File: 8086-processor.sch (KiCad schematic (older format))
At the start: 20 parts

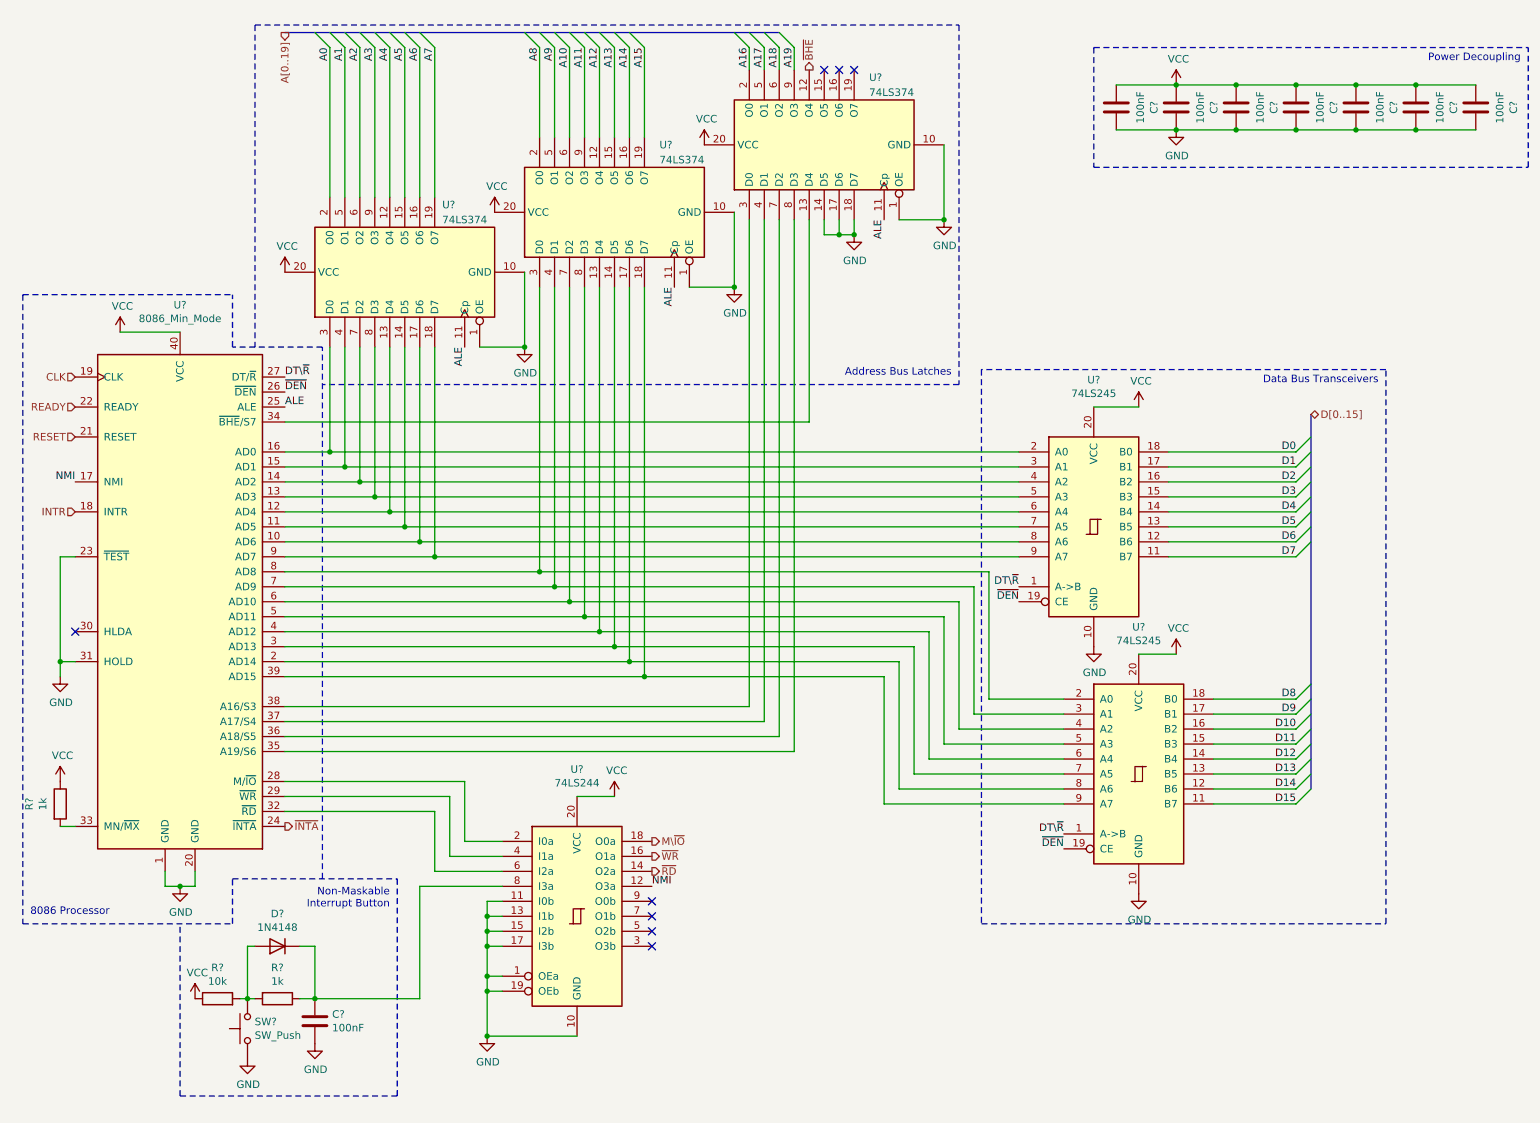
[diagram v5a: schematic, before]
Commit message: Assign footprints for most symbols
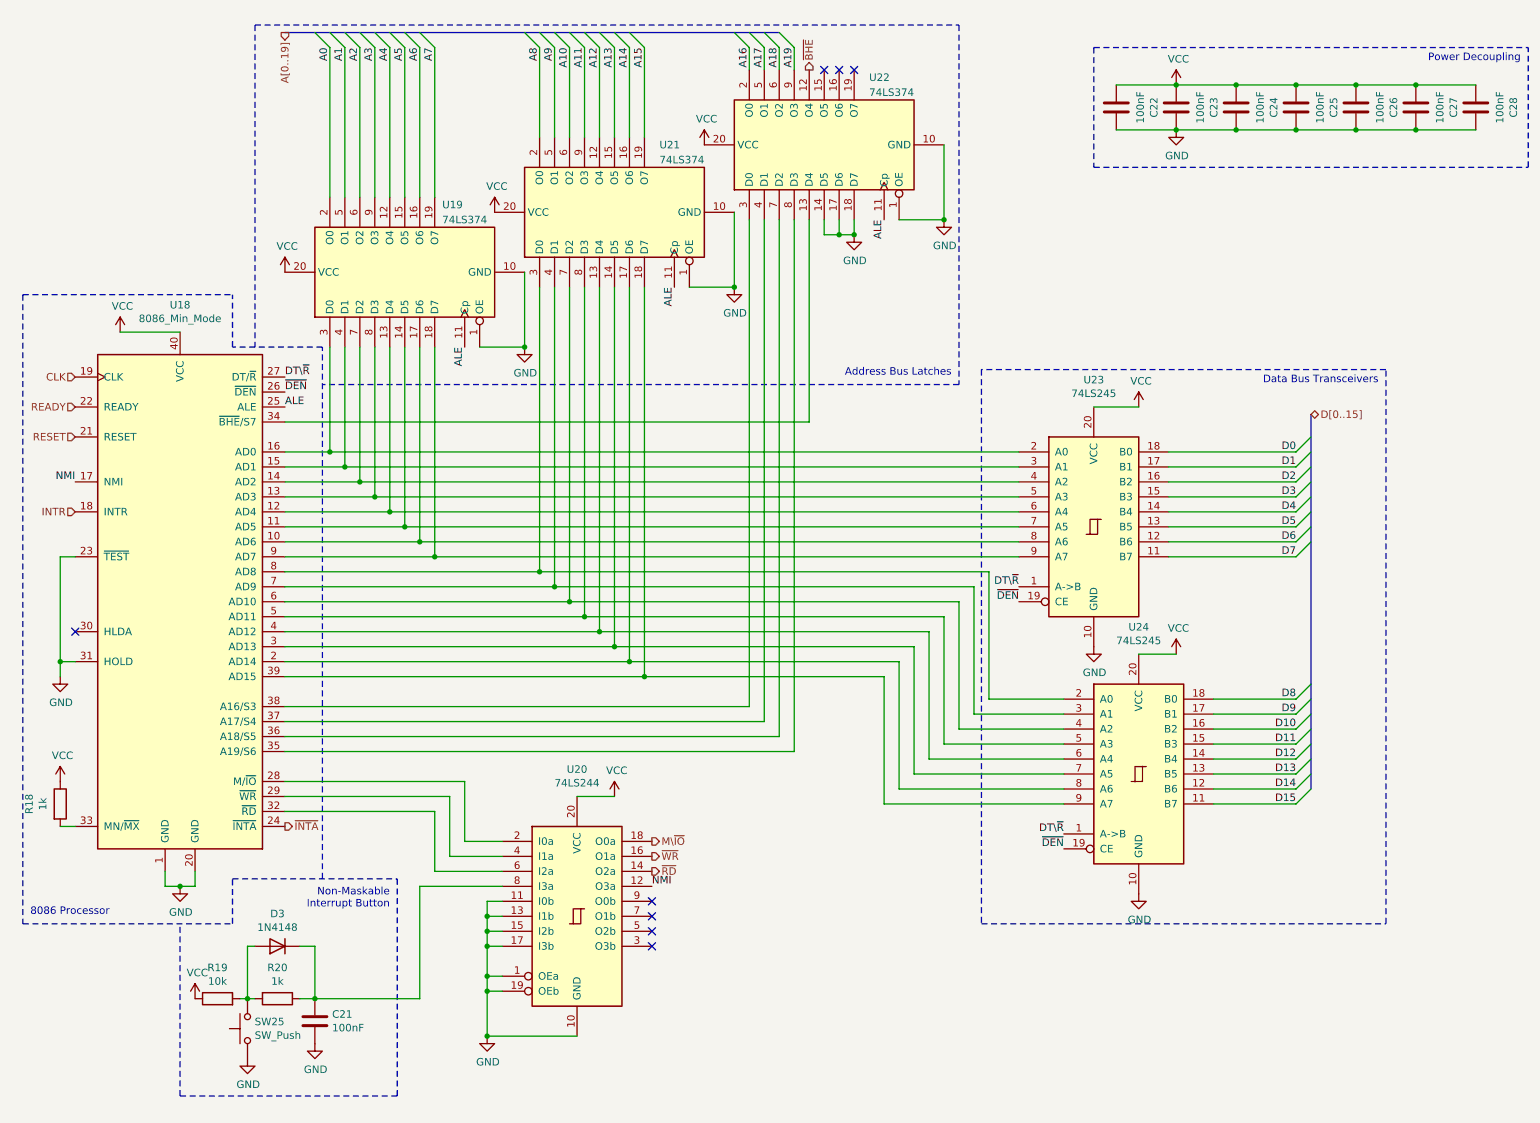
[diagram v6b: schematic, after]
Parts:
- C21, C22, C23, C24, C25, C26, C27, C28: renamed from C?; footprint (none) -> Capacitor_THT:C_Rect_L4.0mm_W2.5mm_P2.50mm
- R18, R19, R20: renamed from R?; footprint (none) -> Resistor_THT:R_Axial_DIN0207_L6.3mm_D2.5mm_P10.16mm_Horizontal
- SW25: renamed from SW?; footprint (none) -> Button_Switch_Keyboard:SW_Cherry_MX_1.00u_PCB
- U19, U20, U21, U22, U23, U24: renamed from U?; footprint (none) -> Package_DIP:DIP-20_W7.62mm
- gave numbers to parts that had none: 2

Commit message: assign footprints and edits
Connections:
- net GND: now also R19.1; no longer C21.2, SW25.1
- net VCC: now also C21.1, SW25.2; no longer R19.1
- net at R20.1, U20.8 (I3a): now also C21.2, D3.2 (A); no longer C21.1, D3.1 (K)
- net at R19.2, R20.2: now also D3.1 (K), SW25.1; no longer D3.2 (A), SW25.2
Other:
- moved on the sheet: C21, D3, SW25
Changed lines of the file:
@@
 	2300 7000 2250 7000
-$Comp
-L power:GND #PWR0191
-U 1 1 627AC8BB
-P 2700 7300
-F 0 "#PWR0191" H 2700 7050 50  0001 C CNN
-F 1 "GND" H 2705 7127 50  0000 C CNN
-F 2 "" H 2700 7300 50  0001 C CNN
-F 3 "" H 2700 7300 50  0001 C CNN
-	1    2700 7300
-	1    0    0    -1
-$EndComp
 $Comp
 L Device:R R20
@@
 F 3 "~" H 2450 7000 50  0001 C CNN
 	1    2450 7000
-	0    1    1    0
+	0    1    -1   0
 $EndComp
 $Comp
 L power:VCC #PWR0192
 U 1 1 6278DB4C
-P 1900 7000
-F 0 "#PWR0192" H 1900 6850 50  0001 C CNN
-F 1 "VCC" H 1915 7173 50  0000 C CNN
-F 2 "" H 1900 7000 50  0001 C CNN
-F 3 "" H 1900 7000 50  0001 C CNN
-	1    1900 7000
+P 2700 6700
+F 0 "#PWR0192" H 2700 6550 50  0001 C CNN
+F 1 "VCC" H 2715 6873 50  0000 C CNN
+F 2 "" H 2700 6700 50  0001 C CNN
+F 3 "" H 2700 6700 50  0001 C CNN
+	1    2700 6700
 	1    0    0    -1
 $EndComp
@@
 L Device:C C21
 U 1 1 6277FDCA
-P 2700 7150
-F 0 "C21" H 2815 7196 50  0000 L CNN
-F 1 "100nF" H 2815 7105 50  0000 L CNN
-F 2 "Capacitor_THT:C_Rect_L4.0mm_W2.5mm_P2.50mm" H 2738 7000 50  0001 C CNN
-F 3 "~" H 2700 7150 50  0001 C CNN
-	1    2700 7150
+P 2700 6850
+F 0 "C21" H 2815 6896 50  0000 L CNN
+F 1 "100nF" H 2815 6805 50  0000 L CNN
+F 2 "Capacitor_THT:C_Rect_L4.0mm_W2.5mm_P2.50mm" H 2738 6700 50  0001 C CNN
+F 3 "~" H 2700 6850 50  0001 C CNN
+	1    2700 6850
 	1    0    0    -1
 $EndComp
@@
 L Switch:SW_Push SW25
 U 1 1 626B0BE8
-P 2250 7200
-F 0 "SW25" V 2296 7152 50  0000 R CNN
-F 1 "SW_Push" V 2205 7152 50  0000 R CNN
-F 2 "Button_Switch_Keyboard:SW_Cherry_MX_1.00u_PCB" H 2250 7400 50  0001 C CNN
-F 3 "~" H 2250 7400 50  0001 C CNN
-	1    2250 7200
+P 2250 6800
+F 0 "SW25" V 2296 6752 50  0000 R CNN
+F 1 "SW_Push" V 2205 6752 50  0000 R CNN
+F 2 "Button_Switch_Keyboard:SW_Cherry_MX_1.00u_PCB" H 2250 7000 50  0001 C CNN
+F 3 "~" H 2250 7000 50  0001 C CNN
+	1    2250 6800
 	0    -1   -1   0
 $EndComp
@@
 L power:GND #PWR0193
 U 1 1 6233B1ED
-P 2250 7400
-F 0 "#PWR0193" H 2250 7150 50  0001 C CNN
-F 1 "GND" H 2255 7227 50  0000 C CNN
-F 2 "" H 2250 7400 50  0001 C CNN
-F 3 "" H 2250 7400 50  0001 C CNN
-	1    2250 7400
+P 1900 7100
+F 0 "#PWR0193" H 1900 6850 50  0001 C CNN
+F 1 "GND" H 1905 6927 50  0000 C CNN
+F 2 "" H 1900 7100 50  0001 C CNN
+F 3 "" H 1900 7100 50  0001 C CNN
+	1    1900 7100
 	1    0    0    -1
 $EndComp
@@
 L Diode:1N4148 D?
 U 1 1 61F82EF7
-P 2450 6650
+P 2450 7350
 AR Path="/61CB92C1/61F82EF7" Ref="D?"  Part="1"
 AR Path="/6190420C/61F82EF7" Ref="D3"  Part="1"
-F 0 "D3" H 2450 6433 50  0000 C CNN
-F 1 "1N4148" H 2450 6524 50  0000 C CNN
-F 2 "Diode_THT:D_DO-35_SOD27_P7.62mm_Horizontal" H 2450 6475 50  0001 C CNN
-F 3 "https://assets.nexperia.com/documents/data-sheet/1N4148_1N4448.pdf" H 2450 6650 50  0001 C CNN
-	1    2450 6650
-	-1   0    0    1
+F 0 "D3" H 2450 7133 50  0000 C CNN
+F 1 "1N4148" H 2450 7224 50  0000 C CNN
+F 2 "Diode_THT:D_DO-35_SOD27_P7.62mm_Horizontal" H 2450 7175 50  0001 C CNN
+F 3 "https://assets.nexperia.com/documents/data-sheet/1N4148_1N4448.pdf" H 2450 7350 50  0001 C CNN
+	1    2450 7350
+	1    0    0    -1
 $EndComp
 Wire Notes Line
@@
 Wire Notes Line
 	3250 7650 3250 6200
-Wire Wire Line
-	2600 6650 2700 6650
-Wire Wire Line
-	2300 6650 2250 6650
-Wire Wire Line
-	2250 6650 2250 7000
-Wire Wire Line
-	2700 6650 2700 7000
 Wire Wire Line
 	1100 4050 1000 4050
@@
 	1000 4850 1000 4750
 NoConn ~ 1100 4550
+$Comp
+L power:VCC #PWR04
+U 1 1 61B699AA
+P 2250 6600
+F 0 "#PWR04" H 2250 6450 50  0001 C CNN
+F 1 "VCC" H 2265 6773 50  0000 C CNN
+F 2 "" H 2250 6600 50  0001 C CNN
+F 3 "" H 2250 6600 50  0001 C CNN
+	1    2250 6600
+	1    0    0    -1
+$EndComp
+Wire Wire Line
+	2700 7000 2700 7350
+Wire Wire Line
+	2700 7350 2600 7350
+Wire Wire Line
+	2250 7000 2250 7350
+Wire Wire Line
+	2250 7350 2300 7350
+Wire Wire Line
+	1900 7100 1900 7000
 Wire Bus Line
 	9350 3100 9350 5600

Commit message: begin pcb layout
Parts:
- SW25: value SW_Push -> NMI
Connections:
- net A0: now also U19.9 (O3); no longer U19.2 (O0)
- net A1: now also U19.6 (O2); no longer U19.5 (O1)
- net A10: now also U21.5 (O1); no longer U21.6 (O2)
- net A11: now also U21.2 (O0); no longer U21.9 (O3)
- net A2: now also U19.5 (O1); no longer U19.6 (O2)
- net A3: now also U19.2 (O0); no longer U19.9 (O3)
- net A8: now also U21.9 (O3); no longer U21.2 (O0)
- net A9: now also U21.6 (O2); no longer U21.5 (O1)
- net at U18.13 (AD3), U23.5 (A3): now also U19.3 (D0); no longer U19.8 (D3)
- net at U18.14 (AD2), U23.4 (A2): now also U19.4 (D1); no longer U19.7 (D2)
- net at U18.15 (AD1), U23.3 (A1): now also U19.7 (D2); no longer U19.4 (D1)
- net at U18.16 (AD0), U23.2 (A0): now also U19.8 (D3); no longer U19.3 (D0)
- net at U18.5 (AD11), U24.5 (A3): now also U21.3 (D0); no longer U21.8 (D3)
- net at U18.6 (AD10), U24.4 (A2): now also U21.4 (D1); no longer U21.7 (D2)
- net at U18.7 (AD9), U24.3 (A1): now also U21.7 (D2); no longer U21.4 (D1)
- net at U18.8 (AD8), U24.2 (A0): now also U21.8 (D3); no longer U21.3 (D0)
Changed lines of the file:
@@
 ALE
 Wire Wire Line
-	2500 3750 3200 3750
-Wire Wire Line
 	6600 5600 7700 5600
 Wire Wire Line
@@
 Wire Wire Line
 	6500 4850 6500 5700
-Wire Wire Line
-	3100 2650 3100 3650
-Wire Wire Line
-	3000 2650 3000 3550
 $Comp
 L power:VCC #PWR0181
@@
 $EndComp
 Wire Wire Line
-	2800 2650 2800 3350
-Wire Wire Line
-	2900 2650 2900 3450
-Wire Wire Line
 	3800 2650 4100 2650
 Connection ~ 4100 2650
@@
 ALE
 Wire Wire Line
-	2500 3650 3100 3650
-Wire Wire Line
-	2500 3450 2900 3450
-Wire Wire Line
-	2500 3350 2800 3350
-Wire Wire Line
-	2500 3550 3000 3550
-Connection ~ 2800 3350
-Wire Wire Line
-	2800 3350 7400 3350
-Connection ~ 2900 3450
-Wire Wire Line
-	2900 3450 7400 3450
-Connection ~ 3000 3550
-Wire Wire Line
-	3000 3550 7400 3550
-Connection ~ 3100 3650
-Wire Wire Line
-	3100 3650 7400 3650
+	2500 3650 2800 3650
+Wire Wire Line
+	2500 3550 2900 3550
 Wire Wire Line
 	5600 1800 5600 5050
@@
 	5900 5350 2500 5350
 Wire Wire Line
-	2500 3850 3300 3850
-Wire Wire Line
-	2500 3950 3400 3950
-Wire Wire Line
-	2500 4050 3500 4050
-Wire Wire Line
-	2500 4150 4200 4150
-Wire Wire Line
-	2500 4250 4300 4250
-Wire Wire Line
-	2500 4350 4400 4350
-Wire Wire Line
-	2500 4650 4700 4650
-Wire Wire Line
-	2500 4850 4900 4850
-Wire Wire Line
-	3200 2650 3200 3750
-Connection ~ 3200 3750
-Wire Wire Line
-	3200 3750 7400 3750
-Wire Wire Line
-	3300 3850 3300 2650
-Connection ~ 3300 3850
-Wire Wire Line
-	3300 3850 7400 3850
-Wire Wire Line
-	3400 2650 3400 3950
-Connection ~ 3400 3950
-Wire Wire Line
-	3400 3950 7400 3950
-Wire Wire Line
-	3500 4050 3500 2650
-Connection ~ 3500 4050
-Wire Wire Line
-	3500 4050 7400 4050
-Wire Wire Line
-	2500 4750 4800 4750
-Wire Wire Line
-	2500 4550 4600 4550
-Wire Wire Line
-	2500 4450 4500 4450
-Wire Wire Line
-	4200 4150 4200 2250
-Connection ~ 4200 4150
-Connection ~ 4300 4250
-Connection ~ 4400 4350
-Connection ~ 4500 4450
-Connection ~ 4600 4550
-Connection ~ 4700 4650
-Connection ~ 4800 4750
-Wire Wire Line
-	4800 4750 6600 4750
-Wire Wire Line
-	4900 2250 4900 4850
-Connection ~ 4900 4850
-Wire Wire Line
-	4900 4850 6500 4850
-Wire Wire Line
-	4800 2250 4800 4750
-Wire Wire Line
-	4700 4650 6700 4650
-Wire Wire Line
-	4700 2250 4700 4650
-Wire Wire Line
-	4600 4550 6800 4550
-Wire Wire Line
-	4600 2250 4600 4550
-Wire Wire Line
-	4500 4450 6900 4450
-Wire Wire Line
-	4500 2250 4500 4450
-Wire Wire Line
-	4400 4350 7000 4350
-Wire Wire Line
-	4400 2250 4400 4350
-Wire Wire Line
-	4300 4250 7100 4250
-Wire Wire Line
-	4300 2250 4300 4250
-Wire Wire Line
-	4200 4150 7200 4150
+	2500 4350 4300 4350
+Wire Wire Line
+	2500 4450 4200 4450
+Wire Wire Line
+	4500 4150 4500 2250
+Wire Wire Line
+	4400 2250 4400 4250
 $Comp
 L power:VCC #PWR0185
@@
 Entry Wire Line
 	2800 650  2700 550
+Text Label 3100 650  3    50   ~ 0
+A0
+Text Label 3000 650  3    50   ~ 0
+A1
+Text Label 2900 650  3    50   ~ 0
+A2
 Text Label 2800 650  3    50   ~ 0
-A0
-Text Label 3500 650  3    50   ~ 0
-A7
-Text Label 2900 650  3    50   ~ 0
-A1
-Text Label 3000 650  3    50   ~ 0
-A2
-Text Label 3100 650  3    50   ~ 0
 A3
-Text Label 3200 650  3    50   ~ 0
-A4
-Text Label 3300 650  3    50   ~ 0
-A5
-Text Label 3400 650  3    50   ~ 0
-A6
-Text Label 4200 650  3    50   ~ 0
+Text Label 4500 650  3    50   ~ 0
 A8
+Text Label 4400 650  3    50   ~ 0
+A9
 Text Label 4300 650  3    50   ~ 0
-A9
-Text Label 4400 650  3    50   ~ 0
 A10
-Text Label 4500 650  3    50   ~ 0
-A11
-Text Label 4600 650  3    50   ~ 0
-A12
-Text Label 4700 650  3    50   ~ 0
-A13
-Text Label 4800 650  3    50   ~ 0
-A14
-Text Label 4900 650  3    50   ~ 0
-A15
 Text Label 5600 650  3    50   ~ 0
 A16
@@
 P 2250 6800
 F 0 "SW25" V 2296 6752 50  0000 R CNN
-F 1 "SW_Push" V 2205 6752 50  0000 R CNN
+F 1 "NMI" V 2205 6752 50  0000 R CNN
 F 2 "Button_Switch_Keyboard:SW_Cherry_MX_1.00u_PCB" H 2250 7000 50  0001 C CNN
 F 3 "~" H 2250 7000 50  0001 C CNN
@@
 Text Notes 3200 6400 2    50   ~ 0
 Non-Maskable\nInterrupt Button
-Text Label 4950 6250 0    50   ~ 0
-NMI
 $Comp
 L power:GND #PWR0193
@@
 Text HLabel 4950 6150 2    50   Output ~ 0
 ~RD
-NoConn ~ 4950 6350
 NoConn ~ 4950 6450
 NoConn ~ 4950 6550
@@
 	750  6500 2150 6500
 Wire Notes Line
-	2750 6200 2750 2650
-Wire Notes Line
 	2150 6200 3250 6200
 Wire Notes Line
@@
 Wire Wire Line
 	1900 7100 1900 7000
+Text Label 4800 650  3    50   ~ 0
+A14
+Text Label 4700 650  3    50   ~ 0
+A13
+Text Label 4600 650  3    50   ~ 0
+A12
+Text Label 4900 650  3    50   ~ 0
+A15
+Wire Wire Line
+	2500 4550 4600 4550
+Connection ~ 4600 4550
+Wire Wire Line
+	2500 4650 4700 4650
+Connection ~ 4700 4650
+Wire Wire Line
+	4900 4850 6500 4850
+Connection ~ 4900 4850
+Wire Wire Line
+	4800 4750 6600 4750
+Connection ~ 4800 4750
+Wire Wire Line
+	4600 4550 6800 4550
+Wire Wire Line
+	4700 4650 6700 4650
+Wire Wire Line
+	2500 4750 4800 4750
+Wire Wire Line
+	2500 4850 4900 4850
+Wire Wire Line
+	4600 2250 4600 4550
+Wire Wire Line
+	4700 2250 4700 4650
+Wire Wire Line
+	4800 2250 4800 4750
+Wire Wire Line
+	4900 2250 4900 4850
+Text Label 3300 650  3    50   ~ 0
+A5
+Text Label 3400 650  3    50   ~ 0
+A6
+Text Label 3500 650  3    50   ~ 0
+A7
+Wire Wire Line
+	2500 3750 3200 3750
+Connection ~ 3200 3750
+Wire Wire Line
+	2500 3850 3300 3850
+Connection ~ 3300 3850
+Text Label 3200 650  3    50   ~ 0
+A4
+Wire Wire Line
+	3500 4050 7400 4050
+Connection ~ 3500 4050
+Wire Wire Line
+	3400 3950 7400 3950
+Connection ~ 3400 3950
+Wire Wire Line
+	3200 3750 7400 3750
+Wire Wire Line
+	3300 3850 7400 3850
+Wire Wire Line
+	2500 3950 3400 3950
+Wire Wire Line
+	2500 4050 3500 4050
+Wire Wire Line
+	3500 4050 3500 2650
+Wire Wire Line
+	3400 2650 3400 3950
+Wire Wire Line
+	3300 3850 3300 2650
+Wire Wire Line
+	3200 2650 3200 3750
+Wire Notes Line
+	2750 6200 2750 2650
+Wire Wire Line
+	3000 2650 3000 3450
+Wire Wire Line
+	3100 2650 3100 3350
+Connection ~ 2800 3650
+Connection ~ 2900 3550
+Connection ~ 3000 3450
+Wire Wire Line
+	3000 3450 7400 3450
+Connection ~ 3100 3350
+Wire Wire Line
+	3100 3350 7400 3350
+Wire Wire Line
+	2900 3550 7400 3550
+Wire Wire Line
+	2800 3650 7400 3650
+Wire Wire Line
+	2500 3350 3100 3350
+Wire Wire Line
+	2800 2650 2800 3650
+Wire Wire Line
+	2500 3450 3000 3450
+Wire Wire Line
+	2900 2650 2900 3550
+Connection ~ 4200 4450
+Connection ~ 4300 4350
+Connection ~ 4400 4250
+Wire Wire Line
+	4400 4250 7100 4250
+Connection ~ 4500 4150
+Wire Wire Line
+	4500 4150 7200 4150
+Wire Wire Line
+	4200 4450 6900 4450
+Wire Wire Line
+	4300 4350 7000 4350
+Wire Wire Line
+	2500 4150 4500 4150
+Wire Wire Line
+	4200 2250 4200 4450
+Wire Wire Line
+	2500 4250 4400 4250
+Wire Wire Line
+	4300 2250 4300 4350
+Text Label 4200 650  3    50   ~ 0
+A11
+Text Label 4950 6250 0    50   ~ 0
+NMI
+NoConn ~ 4950 6350
 Wire Bus Line
 	9350 3100 9350 5600
